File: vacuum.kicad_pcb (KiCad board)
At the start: 2 copper layers, 94 x 94 mm, 69 parts, among them J1 к БП, J10 геркон шибера 1, J11 запасной, J12 запасной, J13 к БП, J2 нагрузка, J3 нагрузка, J4 геркон клапана 0, J5 нагрузка, J6 нагрузка, J7 к БП, J8 геркон клапана 1, J9 геркон шибера 0, Q1 IRF740, Q2 IRF740, Q3 IRF740, Q4 IRF740, SW1 Кнопка, SW2 Кнопка, SW3 Кнопка, SW4 Выключить автоматику, SW5 Кнопка, U1 PC817, U10 PC817, U2 PC817, U3 PC817, U4 PC817, U5 PC817, U6 PC817, U7 PC817, U8 PC817, U9 PC817

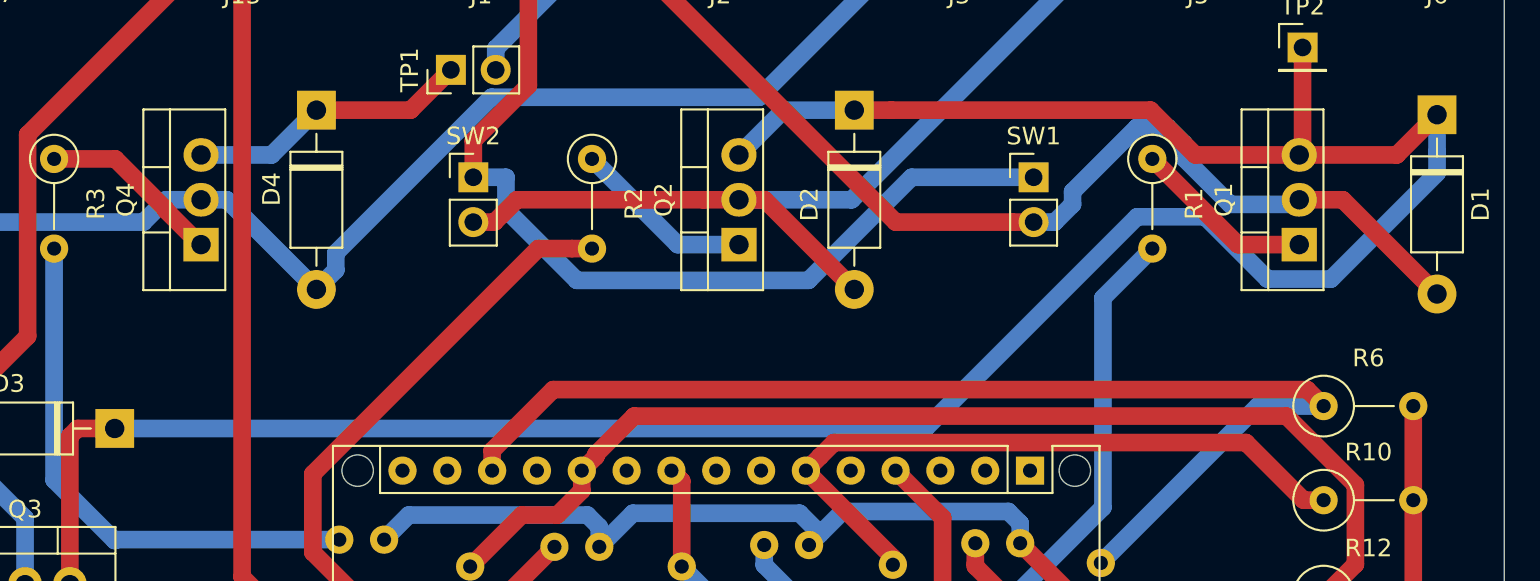
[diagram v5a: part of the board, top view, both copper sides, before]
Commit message: capasitor added to reset pin of Arduino dor DTR disabling
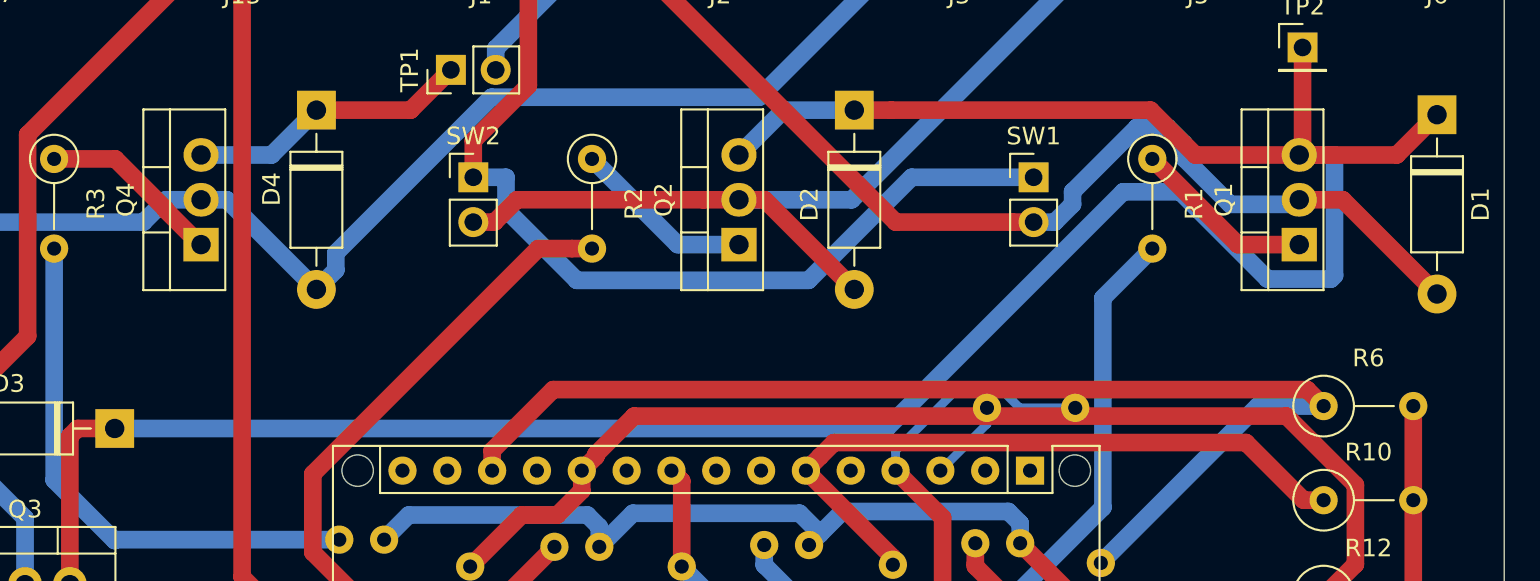
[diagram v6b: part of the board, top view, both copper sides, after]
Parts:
- added C1: 10 мкФ, Capacitor_THT:C_Disc_D6.0mm_W2.5mm_P5.00mm, B.Cu at (128.2, 110.6)
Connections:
- A1 pad 1: Net-(A1-Pad1) -> (no net)
- A1 pad 10: Net-(A1-Pad10) -> (no net)
- A1 pad 12: Net-(A1-Pad12) -> (no net)
- A1 pad 14: Net-(A1-Pad14) -> (no net)
- A1 pad 15: Net-(A1-Pad15) -> (no net)
- A1 pad 16: Net-(A1-Pad16) -> (no net)
- A1 pad 17: Net-(A1-Pad17) -> (no net)
- A1 pad 18: Net-(A1-Pad18) -> (no net)
- A1 pad 19: Net-(A1-Pad19) -> (no net)
- A1 pad 2: Net-(A1-Pad2) -> (no net)
- A1 pad 26: Net-(A1-Pad26) -> (no net)
- A1 pad 28: Net-(A1-Pad28) -> (no net)
- A1 pad 29: Net-(A1-Pad29) -> (no net)
- A1 pad 30: Net-(A1-Pad30) -> (no net)
- A1 pad 5: Net-(A1-Pad5) -> (no net)
- A1 pad 7: Net-(A1-Pad7) -> (no net)
- A1 pad 8: Net-(A1-Pad8) -> (no net)
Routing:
- net Net-(A1-Pad4): track 201.8 -> 215.2 mm
- net Net-(A1-Pad3): track 0.00 -> 4.65 mm
- net Net-(D1-Pad1): track 188.9 -> 187.4 mm

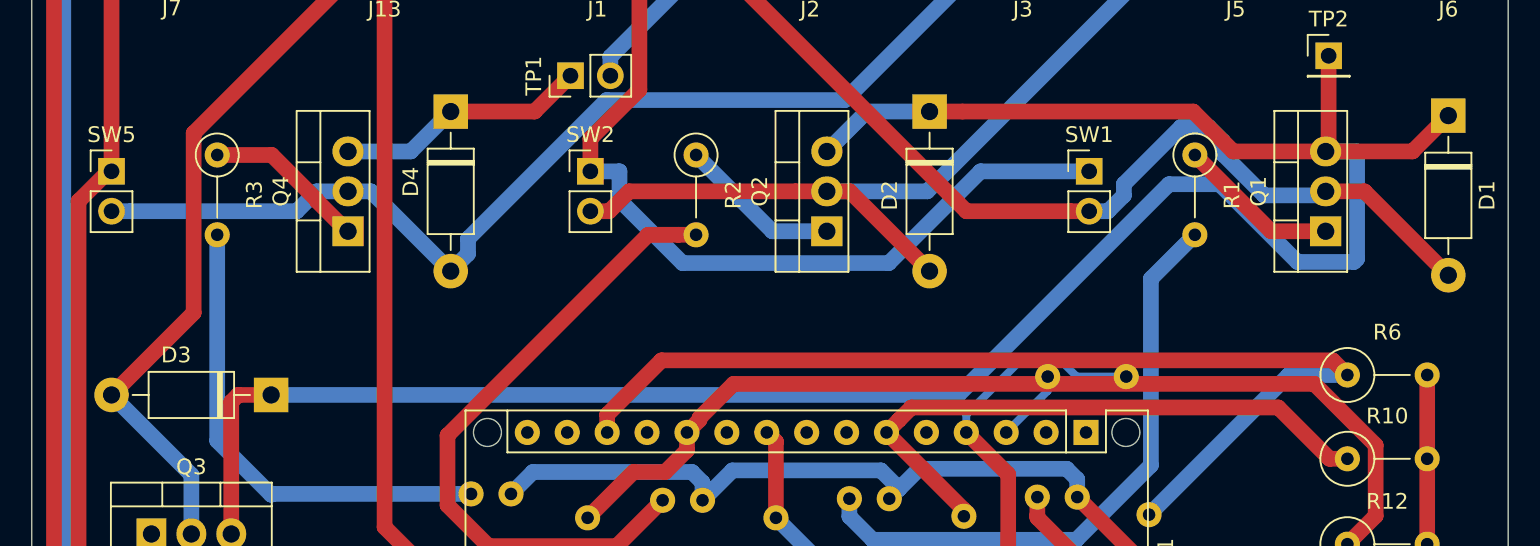
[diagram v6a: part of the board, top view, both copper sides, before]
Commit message: diods direction changed to correct
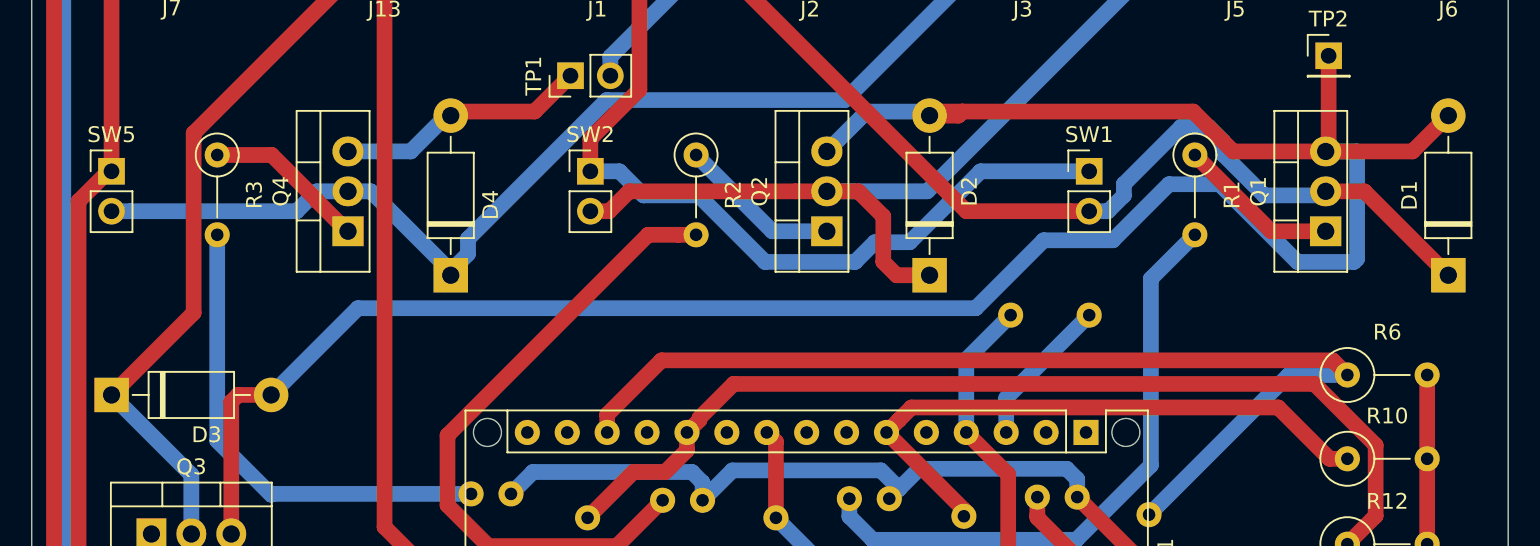
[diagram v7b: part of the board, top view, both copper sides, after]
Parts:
- moved D2 10.4 mm to (120.7, 104.1), turned to 90 degrees
- moved D4 10.4 mm to (90.2, 104.1), turned to 90 degrees
- moved D1 10.2 mm to (153.7, 104.1), turned to 90 degrees
- moved D3 10.2 mm to (68.6, 111.8), turned to 0 degrees
- moved C1 4.72 mm to (130.8, 106.7), turned to 180 degrees
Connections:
- A1 pad 1: (no net) -> Net-(A1-Pad1)
- A1 pad 10: (no net) -> Net-(A1-Pad10)
- A1 pad 12: (no net) -> Net-(A1-Pad12)
- A1 pad 14: (no net) -> Net-(A1-Pad14)
- A1 pad 15: (no net) -> Net-(A1-Pad15)
- A1 pad 16: (no net) -> Net-(A1-Pad16)
- A1 pad 17: (no net) -> Net-(A1-Pad17)
- A1 pad 18: (no net) -> Net-(A1-Pad18)
- A1 pad 19: (no net) -> Net-(A1-Pad19)
- A1 pad 2: (no net) -> Net-(A1-Pad2)
- A1 pad 26: (no net) -> Net-(A1-Pad26)
- A1 pad 28: (no net) -> Net-(A1-Pad28)
- A1 pad 29: (no net) -> Net-(A1-Pad29)
- A1 pad 30: (no net) -> Net-(A1-Pad30)
- A1 pad 5: (no net) -> Net-(A1-Pad5)
- A1 pad 7: (no net) -> Net-(A1-Pad7)
- A1 pad 8: (no net) -> Net-(A1-Pad8)
- D2 pad 1: Net-(D1-Pad1) -> Net-(D2-Pad1)
- D2 pad 2: Net-(D2-Pad2) -> Net-(D1-Pad2)
- D3 pad 1: Net-(D1-Pad1) -> Net-(D3-Pad1)
- D3 pad 2: Net-(D3-Pad2) -> Net-(D1-Pad2)
- J2 pad 2: Net-(D1-Pad2) -> Net-(D1-Pad1)
- J3 pad 2: Net-(D3-Pad2) -> Net-(D3-Pad1)
- J5 pad 2: Net-(D2-Pad2) -> Net-(D2-Pad1)
- J6 pad 2: Net-(D4-Pad2) -> Net-(D4-Pad1)
- Q1 pad 2: Net-(D1-Pad2) -> Net-(D1-Pad1)
- Q1 pad 3: Net-(D1-Pad1) -> Net-(D1-Pad2)
- Q2 pad 2: Net-(D2-Pad2) -> Net-(D2-Pad1)
- Q2 pad 3: Net-(D1-Pad1) -> Net-(D1-Pad2)
- Q3 pad 2: Net-(D3-Pad2) -> Net-(D3-Pad1)
- Q3 pad 3: Net-(D1-Pad1) -> Net-(D1-Pad2)
- Q4 pad 2: Net-(D4-Pad2) -> Net-(D4-Pad1)
- Q4 pad 3: Net-(D4-Pad1) -> Net-(D4-Pad2)
- SW1 pad 2: Net-(D1-Pad2) -> Net-(D1-Pad1)
- SW2 pad 2: Net-(D2-Pad2) -> Net-(D2-Pad1)
- SW3 pad 2: Net-(D3-Pad2) -> Net-(D3-Pad1)
- SW4 pad 1: Net-(D1-Pad1) -> Net-(D1-Pad2)
- SW5 pad 2: Net-(D4-Pad2) -> Net-(D4-Pad1)
- TP1 pad 1: Net-(D4-Pad1) -> Net-(D4-Pad2)
- TP1 pad 2: Net-(D3-Pad2) -> Net-(D3-Pad1)
- TP2 pad 1: Net-(D1-Pad1) -> Net-(D1-Pad2)
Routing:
- net Net-(D3-Pad2): track 132.6 -> 0.00 mm
- net Net-(D3-Pad1): track 0.00 -> 132.6 mm
- net Net-(D1-Pad2): track 64.2 -> 189.6 mm
- net Net-(D1-Pad1): track 187.4 -> 64.2 mm
- net Net-(D4-Pad2): track 95.2 -> 16.2 mm
- net Net-(D4-Pad1): track 16.2 -> 95.2 mm
- net Net-(D2-Pad1): track 0.00 -> 57.3 mm
- net Net-(D2-Pad2): track 55.5 -> 0.00 mm
- net Net-(A1-Pad3): track 4.65 -> 9.66 mm
- net Net-(A1-Pad4): track 215.2 -> 210.5 mm
- net Earth: track 274.4 -> 273.3 mm
